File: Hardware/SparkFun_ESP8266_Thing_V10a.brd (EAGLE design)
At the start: 55.4 x 25.9 mm, 73 parts, among them J1 DNP, Q1 2.5A/30V, U1 ESP8266, U2 MCP73831, U3 AT25SF041-SOIC8, U4 AP2112K-3.3V, U5 DNP, U6 DNP, U7 DNP, Y1 26MHz

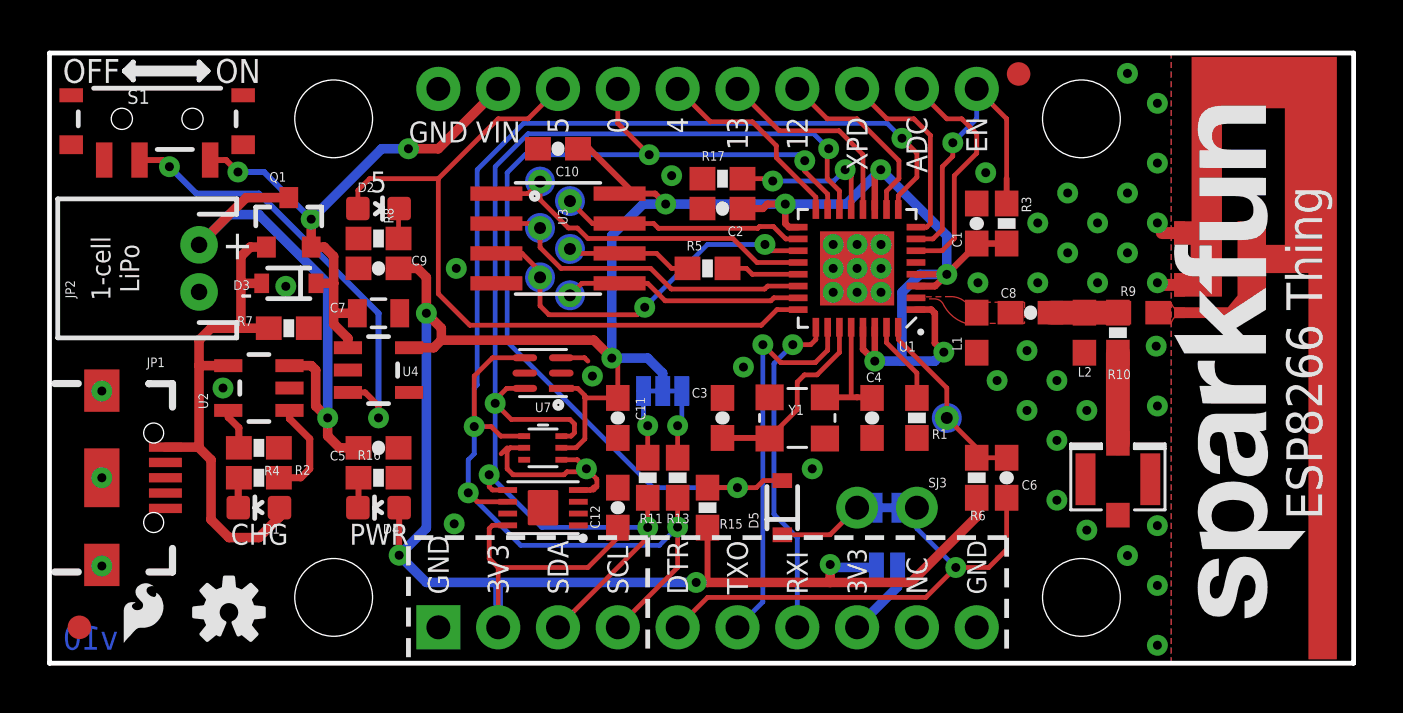
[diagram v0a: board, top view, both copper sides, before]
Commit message: Fix Silkscreen and Copper Width 0 Issue
- Replace Silkscreen for SparkFun, SFE Flame, OSH logo, and RF antenna on individual board and panel with current packages from the SparkFun Eagle Library. By having a defined width for the silkscreen/copper (instead of a "0" width), the CAM job does not generate an "infinite" amount of lines for the polygon => [ [https://learn.sparkfun.com/tutorials/importing-custom-images-into-eagle/#method-1-svg-to-polygon](https://learn.sparkfun.com/tutorials/importing-custom-images-into-eagle/#method-1-svg-to-polygon) ].
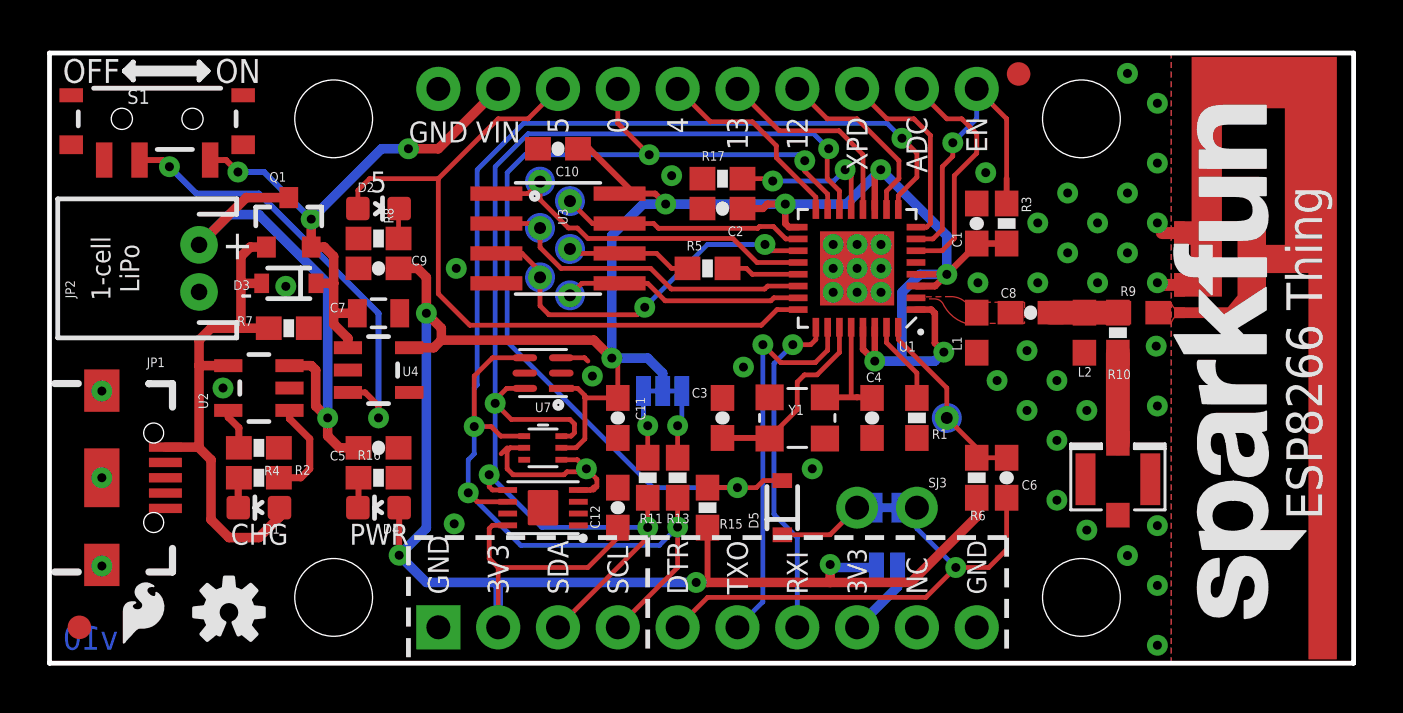
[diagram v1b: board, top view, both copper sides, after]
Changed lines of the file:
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@@
 <layer number="23" name="tOrigins" color="15" fill="1" visible="yes" active="yes"/>
 <layer number="24" name="bOrigins" color="15" fill="1" visible="yes" active="yes"/>
-<layer number="25" name="tNames" color="7" fill="1" visible="yes" active="yes"/>
-<layer number="26" name="bNames" color="7" fill="1" visible="yes" active="yes"/>
-<layer number="27" name="tValues" color="7" fill="1" visible="yes" active="yes"/>
-<layer number="28" name="bValues" color="7" fill="1" visible="yes" active="yes"/>
-<layer number="29" name="tStop" color="7" fill="3" visible="yes" active="yes"/>
-<layer number="30" name="bStop" color="7" fill="6" visible="yes" active="yes"/>
-<layer number="31" name="tCream" color="7" fill="4" visible="yes" active="yes"/>
-<layer number="32" name="bCream" color="7" fill="5" visible="yes" active="yes"/>
-<layer number="33" name="tFinish" color="6" fill="3" visible="yes" active="yes"/>
-<layer number="34" name="bFinish" color="6" fill="6" visible="yes" active="yes"/>
-<layer number="35" name="tGlue" color="7" fill="4" visible="yes" active="yes"/>
-<layer number="36" name="bGlue" color="7" fill="5" visible="yes" active="yes"/>
-<layer number="37" name="tTest" color="7" fill="1" visible="yes" active="yes"/>
-<layer number="38" name="bTest" color="7" fill="1" visible="yes" active="yes"/>
-<layer number="39" name="tKeepout" color="4" fill="11" visible="yes" active="yes"/>
-<layer number="40" name="bKeepout" color="1" fill="11" visible="yes" active="yes"/>
-<layer number="41" name="tRestrict" color="4" fill="10" visible="yes" active="yes"/>
-<layer number="42" name="bRestrict" color="1" fill="10" visible="yes" active="yes"/>
-<layer number="43" name="vRestrict" color="2" fill="10" visible="yes" active="yes"/>
-<layer number="44" name="Drills" color="7" fill="1" visible="yes" active="yes"/>
+<layer number="25" name="tNames" color="7" fill="1" visible="no" active="yes"/>
+<layer number="26" name="bNames" color="7" fill="1" visible="no" active="yes"/>
+<layer number="27" name="tValues" color="7" fill="1" visible="no" active="yes"/>
+<layer number="28" name="bValues" color="7" fill="1" visible="no" active="yes"/>
+<layer number="29" name="tStop" color="7" fill="3" visible="no" active="yes"/>
+<layer number="30" name="bStop" color="7" fill="6" visible="no" active="yes"/>
+<layer number="31" name="tCream" color="7" fill="4" visible="no" active="yes"/>
+<layer number="32" name="bCream" color="7" fill="5" visible="no" active="yes"/>
+<layer number="33" name="tFinish" color="6" fill="3" visible="no" active="yes"/>
+<layer number="34" name="bFinish" color="6" fill="6" visible="no" active="yes"/>
+<layer number="35" name="tGlue" color="7" fill="4" visible="no" active="yes"/>
+<layer number="36" name="bGlue" color="7" fill="5" visible="no" active="yes"/>
+<layer number="37" name="tTest" color="7" fill="1" visible="no" active="yes"/>
+<layer number="38" name="bTest" color="7" fill="1" visible="no" active="yes"/>
+<layer number="39" name="tKeepout" color="4" fill="11" visible="no" active="yes"/>
+<layer number="40" name="bKeepout" color="1" fill="11" visible="no" active="yes"/>
+<layer number="41" name="tRestrict" color="4" fill="10" visible="no" active="yes"/>
+<layer number="42" name="bRestrict" color="1" fill="10" visible="no" active="yes"/>
+<layer number="43" name="vRestrict" color="2" fill="10" visible="no" active="yes"/>
+<layer number="44" name="Drills" color="7" fill="1" visible="no" active="yes"/>
 <layer number="45" name="Holes" color="7" fill="1" visible="yes" active="yes"/>
-<layer number="46" name="Milling" color="3" fill="1" visible="yes" active="yes"/>
-<layer number="47" name="Measures" color="7" fill="1" visible="yes" active="yes"/>
-<layer number="48" name="Document" color="7" fill="1" visible="yes" active="yes"/>
-<layer number="49" name="Reference" color="7" fill="1" visible="yes" active="yes"/>
-<layer number="50" name="dxf" color="7" fill="1" visible="yes" active="yes"/>
+<layer number="46" name="Milling" color="3" fill="1" visible="no" active="yes"/>
+<layer number="47" name="Measures" color="7" fill="1" visible="no" active="yes"/>
+<layer number="48" name="Document" color="7" fill="1" visible="no" active="yes"/>
+<layer number="49" name="Reference" color="7" fill="1" visible="no" active="yes"/>
+<layer number="50" name="dxf" color="7" fill="1" visible="no" active="yes"/>
 <layer number="51" name="tDocu" color="6" fill="1" visible="yes" active="yes"/>
-<layer number="52" name="bDocu" color="7" fill="1" visible="yes" active="yes"/>
+<layer number="52" name="bDocu" color="7" fill="1" visible="no" active="yes"/>
 <layer number="91" name="Nets" color="2" fill="1" visible="no" active="no"/>
 <layer number="92" name="Busses" color="1" fill="1" visible="no" active="no"/>
@@
 <layer number="112" name="tSilk" color="7" fill="1" visible="no" active="no"/>
 <layer number="113" name="IDFDebug" color="7" fill="1" visible="no" active="no"/>
+<layer number="114" name="Badge_Outline" color="7" fill="1" visible="no" active="no"/>
+<layer number="115" name="ReferenceISLANDS" color="7" fill="1" visible="no" active="no"/>
 <layer number="116" name="Patch_BOT" color="9" fill="4" visible="no" active="no"/>
 <layer number="118" name="Rect_Pads" color="7" fill="1" visible="no" active="no"/>
